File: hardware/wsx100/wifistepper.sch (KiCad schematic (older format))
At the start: 59 parts, among them J1 Barrel_Jack_Switch, J2 Screw_Terminal, J3 Conn_01x06, J4 Conn_01x09, J5 Conn_01x02, SW1 SW_SPST, U1 ESP-WROOM-02, U2 powerSTEP01, U3 MAX15062A, U4 ATECC508A

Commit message: Updated hardware and webpage
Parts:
- removed J4: Conn_01x09, Connector_PinHeader_2.54mm:PinHeader_1x09_P2.54mm_Vertical, symbol Connector_Generic:Conn_01x09
- removed R0: 00, Resistor_SMD:R_0805_2012Metric_Pad1.15x1.40mm_HandSolder, symbol Device:R
- removed R2: 1.8K, Resistor_SMD:R_0603_1608Metric, symbol Device:R
- added J4: Conn_01x10, Connector_PinHeader_2.54mm:PinHeader_1x10_P2.54mm_Vertical, symbol Connector_Generic:Conn_01x10
- added JP0, JP3: SolderJumper_2_Bridged, Jumper:SolderJumper-2_P1.3mm_Bridged_RoundedPad1.0x1.5mm, symbol Jumper:SolderJumper_2_Bridged
- added JP4: SolderJumper_3_Bridged12, Jumper:SolderJumper-3_P1.3mm_Bridged12_RoundedPad1.0x1.5mm, symbol Jumper:SolderJumper_3_Bridged12
- added R3: 47K, Resistor_SMD:R_0603_1608Metric, symbol Device:R
- added R4: 1.8K, Resistor_SMD:R_0603_1608Metric, symbol Device:R
- added R5: 2.2K, Resistor_SMD:R_0603_1608Metric, symbol Device:R
- added R6: 1K, Resistor_SMD:R_0603_1608Metric, symbol Device:R
- R1: value 47K -> -; footprint Resistor_SMD:R_0603_1608Metric -> Resistor_SMD:R_0805_2012Metric_Pad1.15x1.40mm_HandSolder
- R14, R15: value 4.7K -> 2.2K
- RS1, RS2, RS3, RS4, RS5, RS6: value 0.06 -> 0.3
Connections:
- net +3V3: now also J4.1 (Pin_1)
- net AUTH_SCK: now also SW1.2 (B), J4.3 (Pin_3)
- net AUTH_SDA: now also J4.4 (Pin_4); no longer SW1.2 (B)
- net GND: now also J4.2 (Pin_2), R4.2, R6.2
- net PROG_BOOT: now also J4.8 (Pin_8)
- net PROG_RX: now also J4.9 (Pin_9)
- net PROG_TX: now also J4.10 (Pin_10)
- net SM_ADC: now also JP4.2 (C), R4.1; no longer R1.2
- net VIN: now also JP0.1 (A), R3.1
- net WIFI_ADC: now also R5.2, R6.1
- net WIFI_CONN: now also JP3.1 (A); no longer U1.17 (IO16)
- net WIFI_RST: now also J4.5 (Pin_5)
- net at U3.1 (VIN), U3.2 (EN/UVLO): now also JP0.2 (B)
- new net: J4.6 (Pin_6), R5.1
- new net: JP4.1 (A), R3.2
- new net: JP4.3 (B), R1.2
- new net WIFI_GPIO: J4.7 (Pin_7), JP3.2 (B), U1.17 (IO16)
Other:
- note added: "12/21/2018"
- note added: "C"
- note removed: "10/28/2018"
- note removed: "B"
- moved on the sheet: C5, R1, R14, R15, SW1

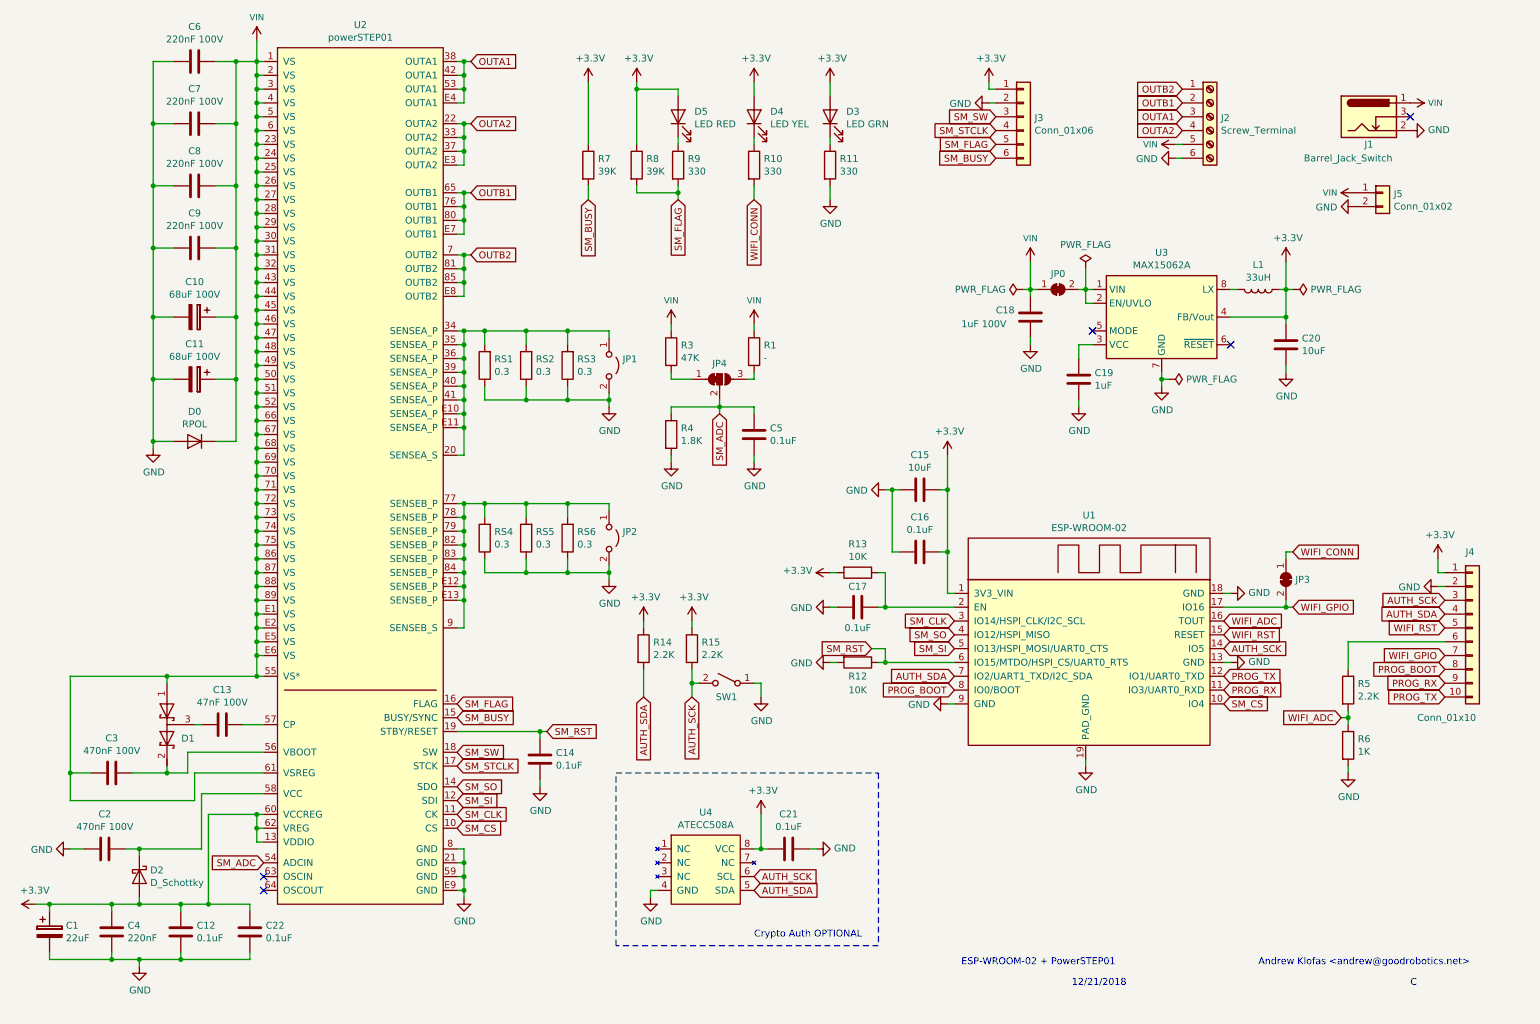
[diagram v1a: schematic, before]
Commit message: Updated hardware to revD (still WIP)
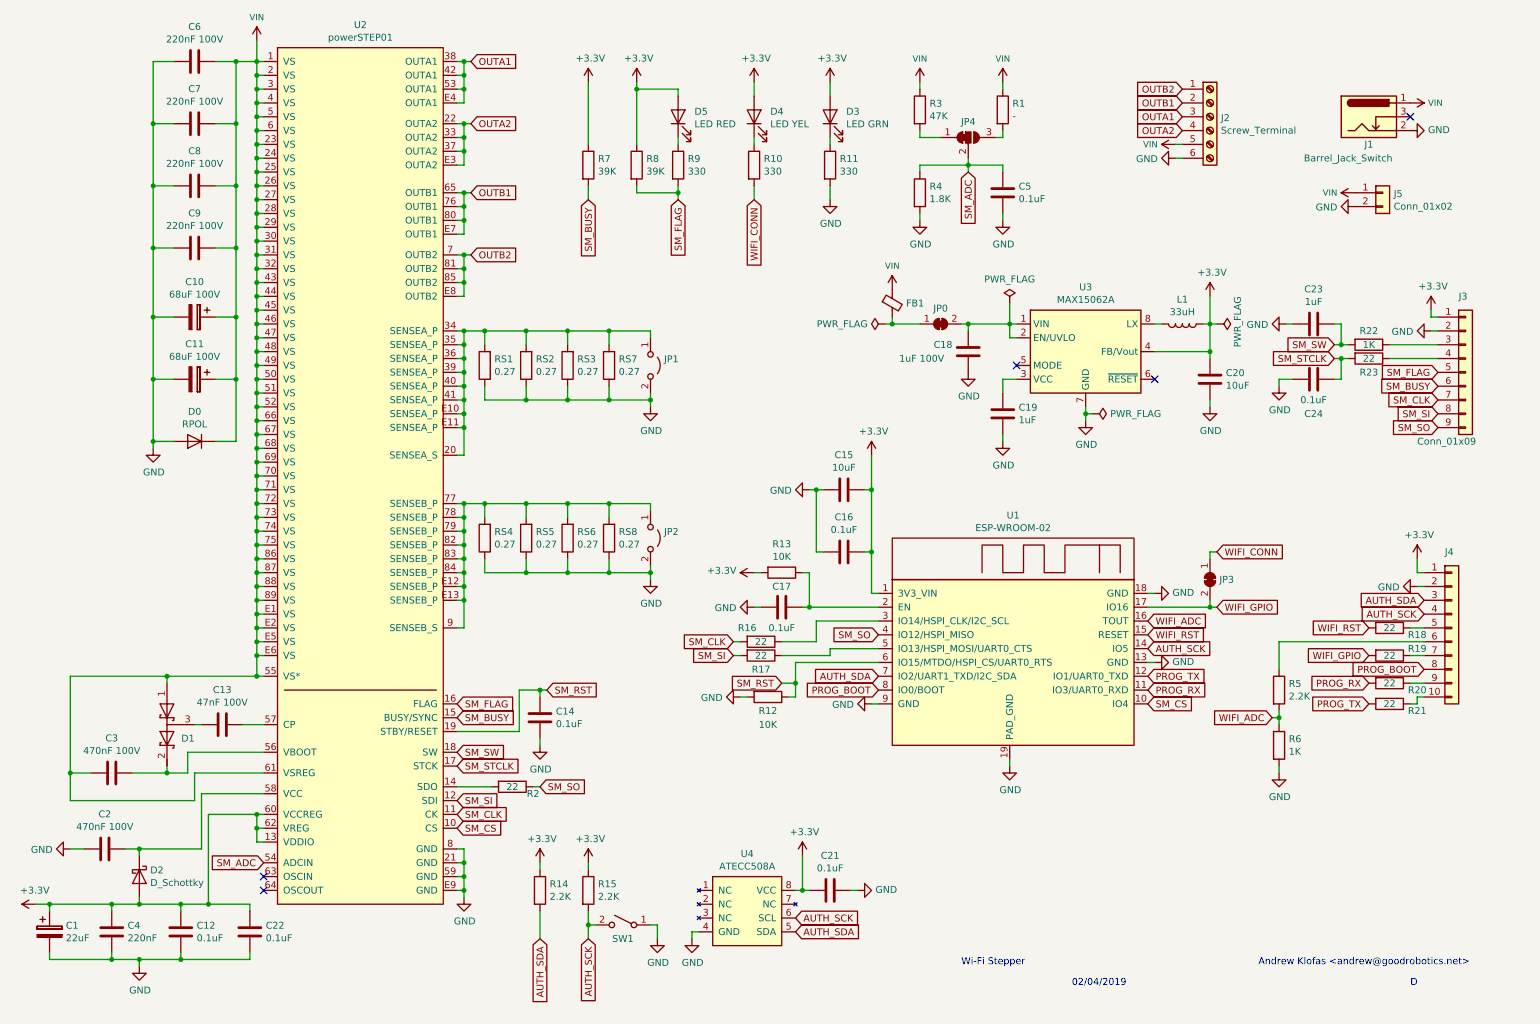
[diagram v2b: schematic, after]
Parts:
- removed J3: Conn_01x06, Connector_PinHeader_2.54mm:PinHeader_1x06_P2.54mm_Vertical, symbol Connector_Generic:Conn_01x06
- added C23: 1uF, Capacitor_SMD:C_0603_1608Metric, symbol Device:C
- added C24: 0.1uF, Capacitor_SMD:C_0603_1608Metric, symbol Device:C
- added FB1: Ferrite_Bead_Small, Inductor_SMD:L_0603_1608Metric, symbol Device:Ferrite_Bead_Small
- added J3: Conn_01x09, Connector_PinHeader_2.54mm:PinHeader_1x09_P2.54mm_Vertical, symbol Connector_Generic:Conn_01x09
- added R16, R17, R18, R19, R2, R20, R21, R23: 22, Resistor_SMD:R_0603_1608Metric, symbol Device:R
- added R22: 1K, Resistor_SMD:R_0603_1608Metric, symbol Device:R
- added RS7, RS8: 0.27, Resistor_SMD:R_2512_6332Metric, symbol Device:R
- C10, C11: footprint Capacitor_THT:CP_Radial_D10.0mm_P5.00mm -> Capacitor_THT:CP_Radial_D12.5mm_P5.00mm
- C18: footprint Capacitor_SMD:C_1206_3216Metric -> Capacitor_SMD:C_0805_2012Metric
- RS1, RS2, RS3, RS4, RS5, RS6: value 0.3 -> 0.27
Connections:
- net +3V3: now also J3.1 (Pin_1)
- net AUTH_SCK: now also J4.4 (Pin_4); no longer J4.3 (Pin_3)
- net AUTH_SDA: now also J4.3 (Pin_3); no longer J4.4 (Pin_4)
- net GND: now also C23.2, C24.2, J3.2 (Pin_2), RS7.1, RS8.1
- net PROG_RX: now also R20.2; no longer J4.9 (Pin_9)
- net PROG_TX: now also R21.2; no longer J4.10 (Pin_10)
- net SM_BUSY: now also J3.6 (Pin_6)
- net SM_CLK: now also J3.7 (Pin_7), R16.2; no longer U1.3 (IO14/HSPI_CLK/I2C_SCL)
- net SM_FLAG: now also J3.5 (Pin_5)
- net SM_SI: now also J3.8 (Pin_8), R17.2; no longer U1.5 (IO13/HSPI_MOSI/UART0_CTS)
- net SM_SO: now also J3.9 (Pin_9), R2.1; no longer U2.14 (SDO)
- net SM_STCLK: now also C24.1, R23.2
- net SM_SW: now also C23.1, R22.2
- net VIN: now also FB1.1; no longer C18.1, JP0.1 (A)
- net WIFI_GPIO: now also R19.2; no longer J4.7 (Pin_7)
- net WIFI_RST: now also R18.2; no longer J4.5 (Pin_5)
- net at JP0.2 (B), U3.1 (VIN), U3.2 (EN/UVLO): now also C18.1
- net at JP1.1 (A), RS1.2, RS2.2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: now also RS7.2
- net at JP2.1 (A), RS4.2, RS5.2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: now also RS8.2
- new net: R16.1, U1.3 (IO14/HSPI_CLK/I2C_SCL)
- new net: R17.1, U1.5 (IO13/HSPI_MOSI/UART0_CTS)
- new net: R2.2, U2.14 (SDO)
- new net: J4.10 (Pin_10), R21.1
- new net: J4.5 (Pin_5), R18.1
- new net: J4.7 (Pin_7), R19.1
- new net: J4.9 (Pin_9), R20.1
- new net: J3.3 (Pin_3), R22.1
- new net: J3.4 (Pin_4), R23.1
- new net: FB1.2, JP0.1 (A)
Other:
- note added: "02/04/2019"
- note added: "D"
- note added: "Wi-Fi Stepper"
- note removed: "12/21/2018"
- note removed: "C"
- note removed: "Crypto Auth OPTIONAL"
- note removed: "ESP-WROOM-02 + PowerSTEP01"
- moved on the sheet: C14, C15, C16, C17, C18, C19, C20, C21, C5, J4, JP0, JP1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

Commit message: Updated Rev D
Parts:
- removed D0: RPOL, Klofas-Passives:D_SOD80, symbol Device:D
- added D0: 80V (Back EMF Clamp), Diode_SMD:D_SOD-123F, symbol Device:D_Schottky
- added D6: 3.9V, Diode_SMD:D_SOD-123, symbol Device:D_Zener
- C10, C11: value 68uF 100V -> 100uF 100V (Low ESR)
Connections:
- net GND: now also D0.2 (A), D6.2 (A)
- net SM_CLK: now also U1.3 (IO14/HSPI_CLK/I2C_SCL); no longer J3.7 (Pin_7)
- net SM_SI: now also U1.5 (IO13/HSPI_MOSI/UART0_CTS); no longer J3.8 (Pin_8)
- net SM_SO: now also R2.2, U2.14 (SDO); no longer J3.9 (Pin_9), R2.1
- net SM_SW: now also D6.1 (K)
- net VIN: now also D0.1 (K)
- net at R16.1: now also J3.7 (Pin_7); no longer U1.3 (IO14/HSPI_CLK/I2C_SCL)
- net at R17.1: now also J3.8 (Pin_8); no longer U1.5 (IO13/HSPI_MOSI/UART0_CTS)
- new net: J3.9 (Pin_9), R2.1
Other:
- moved on the sheet: R16, R17, R2, R21
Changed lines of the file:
@@
 P 1800 2800
 F 0 "C10" V 1545 2800 50  0000 C CNN
-F 1 "68uF 100V" V 1636 2800 50  0000 C CNN
+F 1 "100uF 100V (Low ESR)" V 1650 2650 50  0000 C CNN
 F 2 "Capacitor_THT:CP_Radial_D12.5mm_P5.00mm" H 1838 2650 50  0001 C CNN
 F 3 "~" H 1800 2800 50  0001 C CNN
@@
 P 1800 3250
 F 0 "C11" V 1545 3250 50  0000 C CNN
-F 1 "68uF 100V" V 1636 3250 50  0000 C CNN
+F 1 "100uF 100V (Low ESR)" V 1650 3100 50  0000 C CNN
 F 2 "Capacitor_THT:CP_Radial_D12.5mm_P5.00mm" H 1838 3100 50  0001 C CNN
 F 3 "~" H 1800 3250 50  0001 C CNN
@@
 Connection ~ 1500 3250
 NoConn ~ 2300 6950
-Text GLabel 4300 6200 2    50   Input ~ 0
+Text GLabel 3700 6200 2    50   Input ~ 0
 SM_SO
 Text GLabel 3700 6300 2    50   Input ~ 0
@@
 Text GLabel 10700 5350 0    50   Input ~ 0
 PROG_BOOT
-Text GLabel 10300 5600 0    50   Input ~ 0
+Text GLabel 10300 5550 0    50   Input ~ 0
 PROG_TX
 Text GLabel 10300 5450 0    50   Input ~ 0
@@
 Text GLabel 6750 5100 0    50   Input ~ 0
 SM_SO
-Text GLabel 5700 5250 0    50   Input ~ 0
+Text GLabel 6750 5200 0    50   Input ~ 0
 SM_SI
 $Comp
@@
 	1    0    0    -1
 $EndComp
-$Comp
-L Device:D D0
-U 1 1 5BF7B3E0
-P 1800 3700
-F 0 "D0" H 1800 3484 50  0000 C CNN
-F 1 "RPOL" H 1800 3575 50  0000 C CNN
-F 2 "Klofas-Passives:D_SOD80" H 1800 3700 50  0001 C CNN
-F 3 "~" H 1800 3700 50  0001 C CNN
-	1    1800 3700
-	-1   0    0    1
-$EndComp
 Wire Wire Line
 	1500 3250 1500 3700
@@
 P 11000 3200
 F 0 "J3" H 10950 3750 50  0000 L CNN
-F 1 "Conn_01x09" H 10650 2700 50  0000 L CNN
+F 1 "Conn_01x09" H 10650 2700 50  0001 L CNN
 F 2 "Connector_PinHeader_2.54mm:PinHeader_1x09_P2.54mm_Vertical" H 11000 3200 50  0001 C CNN
 F 3 "~" H 11000 3200 50  0001 C CNN
@@
 	1    0    0    -1
 $EndComp
-Text GLabel 10800 3400 0    50   Input ~ 0
+Text GLabel 10400 3400 0    50   Input ~ 0
 SM_CLK
-Text GLabel 10800 3600 0    50   Input ~ 0
+Text GLabel 10400 3600 0    50   Input ~ 0
 SM_SO
-Text GLabel 10800 3500 0    50   Input ~ 0
+Text GLabel 10400 3500 0    50   Input ~ 0
 SM_SI
 Wire Wire Line
@@
 L Device:R R2
 U 1 1 5C50BF9F
-P 4100 6200
-F 0 "R2" V 4150 6350 50  0000 C CNN
-F 1 "22" V 4100 6200 50  0000 C CNN
-F 2 "Resistor_SMD:R_0603_1608Metric" V 4030 6200 50  0001 C CNN
-F 3 "~" H 4100 6200 50  0001 C CNN
-	1    4100 6200
-	0    1    1    0
-$EndComp
-Wire Wire Line
-	3950 6200 3700 6200
-Wire Wire Line
-	4300 6200 4250 6200
-Wire Wire Line
-	6300 5150 6300 5000
-Wire Wire Line
-	6300 5000 6750 5000
-Wire Wire Line
-	6400 5250 6400 5200
-Wire Wire Line
-	6400 5200 6750 5200
+P 10550 3600
+F 0 "R2" V 10600 3800 50  0000 C CNN
+F 1 "22" V 10550 3600 50  0000 C CNN
+F 2 "Resistor_SMD:R_0603_1608Metric" V 10480 3600 50  0001 C CNN
+F 3 "~" H 10550 3600 50  0001 C CNN
+	1    10550 3600
+	0    1    1    0
+$EndComp
 $Comp
 L Device:R R16
 U 1 1 5C5B87C0
-P 5900 5150
-F 0 "R16" V 5800 5050 50  0000 C CNN
-F 1 "22" V 5900 5150 50  0000 C CNN
-F 2 "Resistor_SMD:R_0603_1608Metric" V 5830 5150 50  0001 C CNN
-F 3 "~" H 5900 5150 50  0001 C CNN
-	1    5900 5150
+P 10550 3400
+F 0 "R16" V 10600 3600 50  0000 C CNN
+F 1 "22" V 10550 3400 50  0000 C CNN
+F 2 "Resistor_SMD:R_0603_1608Metric" V 10480 3400 50  0001 C CNN
+F 3 "~" H 10550 3400 50  0001 C CNN
+	1    10550 3400
 	0    1    1    0
 $EndComp
@@
 L Device:R R17
 U 1 1 5C5B8DA2
-P 5900 5250
-F 0 "R17" V 6000 5250 50  0000 C CNN
-F 1 "22" V 5900 5250 50  0000 C CNN
-F 2 "Resistor_SMD:R_0603_1608Metric" V 5830 5250 50  0001 C CNN
-F 3 "~" H 5900 5250 50  0001 C CNN
-	1    5900 5250
-	0    1    1    0
-$EndComp
-Wire Wire Line
-	5700 5150 5750 5150
-Wire Wire Line
-	5750 5250 5700 5250
-Wire Wire Line
-	6050 5250 6400 5250
-Wire Wire Line
-	6300 5150 6050 5150
+P 10550 3500
+F 0 "R17" V 10600 3700 50  0000 C CNN
+F 1 "22" V 10550 3500 50  0000 C CNN
+F 2 "Resistor_SMD:R_0603_1608Metric" V 10480 3500 50  0001 C CNN
+F 3 "~" H 10550 3500 50  0001 C CNN
+	1    10550 3500
+	0    1    1    0
+$EndComp
 Wire Wire Line
 	5100 3400 5100 3350
@@
 Wire Wire Line
 	4800 3400 5100 3400
-Text GLabel 5700 5150 0    50   Input ~ 0
+Text GLabel 6750 5000 0    50   Input ~ 0
 SM_CLK
 Wire Wire Line
@@
 L Device:R R21
 U 1 1 5CCD98E9
-P 10450 5600
-F 0 "R21" V 10500 5800 50  0000 C CNN
-F 1 "22" V 10450 5600 50  0000 C CNN
-F 2 "Resistor_SMD:R_0603_1608Metric" V 10380 5600 50  0001 C CNN
-F 3 "~" H 10450 5600 50  0001 C CNN
-	1    10450 5600
-	0    1    1    0
-$EndComp
-Wire Wire Line
-	10700 5550 10650 5550
-Wire Wire Line
-	10650 5550 10650 5600
+P 10450 5550
+F 0 "R21" V 10500 5750 50  0000 C CNN
+F 1 "22" V 10450 5550 50  0000 C CNN
+F 2 "Resistor_SMD:R_0603_1608Metric" V 10380 5550 50  0001 C CNN
+F 3 "~" H 10450 5550 50  0001 C CNN
+	1    10450 5550
+	0    1    1    0
+$EndComp
 Wire Wire Line
 	10600 5450 10700 5450
@@
 Wire Wire Line
 	10600 5250 10700 5250
-Wire Wire Line
-	10600 5600 10650 5600
 $Comp
 L Device:R R18
@@
 L power:GND #PWR0138
 U 1 1 5D0D4964
-P 9700 2850
-F 0 "#PWR0138" H 9700 2600 50  0001 C CNN
-F 1 "GND" V 9705 2722 50  0000 R CNN
-F 2 "" H 9700 2850 50  0001 C CNN
-F 3 "" H 9700 2850 50  0001 C CNN
-	1    9700 2850
+P 9650 2450
+F 0 "#PWR0138" H 9650 2200 50  0001 C CNN
+F 1 "GND" V 9655 2322 50  0000 R CNN
+F 2 "" H 9650 2450 50  0001 C CNN
+F 3 "" H 9650 2450 50  0001 C CNN
+	1    9650 2450
 	0    1    1    0
 $EndComp
@@
 Wire Wire Line
 	6850 2850 7050 2850
+Wire Wire Line
+	9650 2450 9700 2450
+Wire Wire Line
+	9700 2450 9700 2850
+Connection ~ 9700 2450
+Wire Wire Line
+	9700 2450 9750 2450
+Wire Wire Line
+	10100 2850 10100 2450
+Wire Wire Line
+	10100 2450 10050 2450
+Connection ~ 10100 2850
+$Comp
+L Device:D_Zener D6
+U 1 1 5C66302D
+P 9900 2450
+F 0 "D6" H 9900 2234 50  0000 C CNN
+F 1 "3.9V" H 9900 2325 50  0000 C CNN
+F 2 "Diode_SMD:D_SOD-123" H 9900 2450 50  0001 C CNN
+F 3 "~" H 9900 2450 50  0001 C CNN
+	1    9900 2450
+	-1   0    0    1
+$EndComp
+Wire Wire Line
+	10700 3500 10800 3500
+Wire Wire Line
+	10700 3600 10800 3600
+Wire Wire Line
+	10600 5550 10700 5550
+Wire Wire Line
+	10700 3400 10800 3400
+$Comp
+L Device:D_Schottky D0
+U 1 1 5C7C4A49
+P 1800 3700
+F 0 "D0" H 1800 3484 50  0000 C CNN
+F 1 "80V (Back EMF Clamp)" H 1950 3600 50  0000 C CNN
+F 2 "Diode_SMD:D_SOD-123F" H 1800 3700 50  0001 C CNN
+F 3 "~" H 1800 3700 50  0001 C CNN
+	1    1800 3700
+	-1   0    0    1
+$EndComp
 $EndSCHEMATC
